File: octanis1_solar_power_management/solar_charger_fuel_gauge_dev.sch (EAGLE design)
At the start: 92 parts, among them IC401 TUSB2046BIRHBIRHB, Q2 32.768kHz, Q4 CSTCR4M00G15L99, Q401 CSTCR6M00G15L99, U1 BQ24210, U2 BQ27510_DRZ_12, U402 TPS62237DRY, U404 TPD2E001DRLR, U6 MSP430F5529IPNR

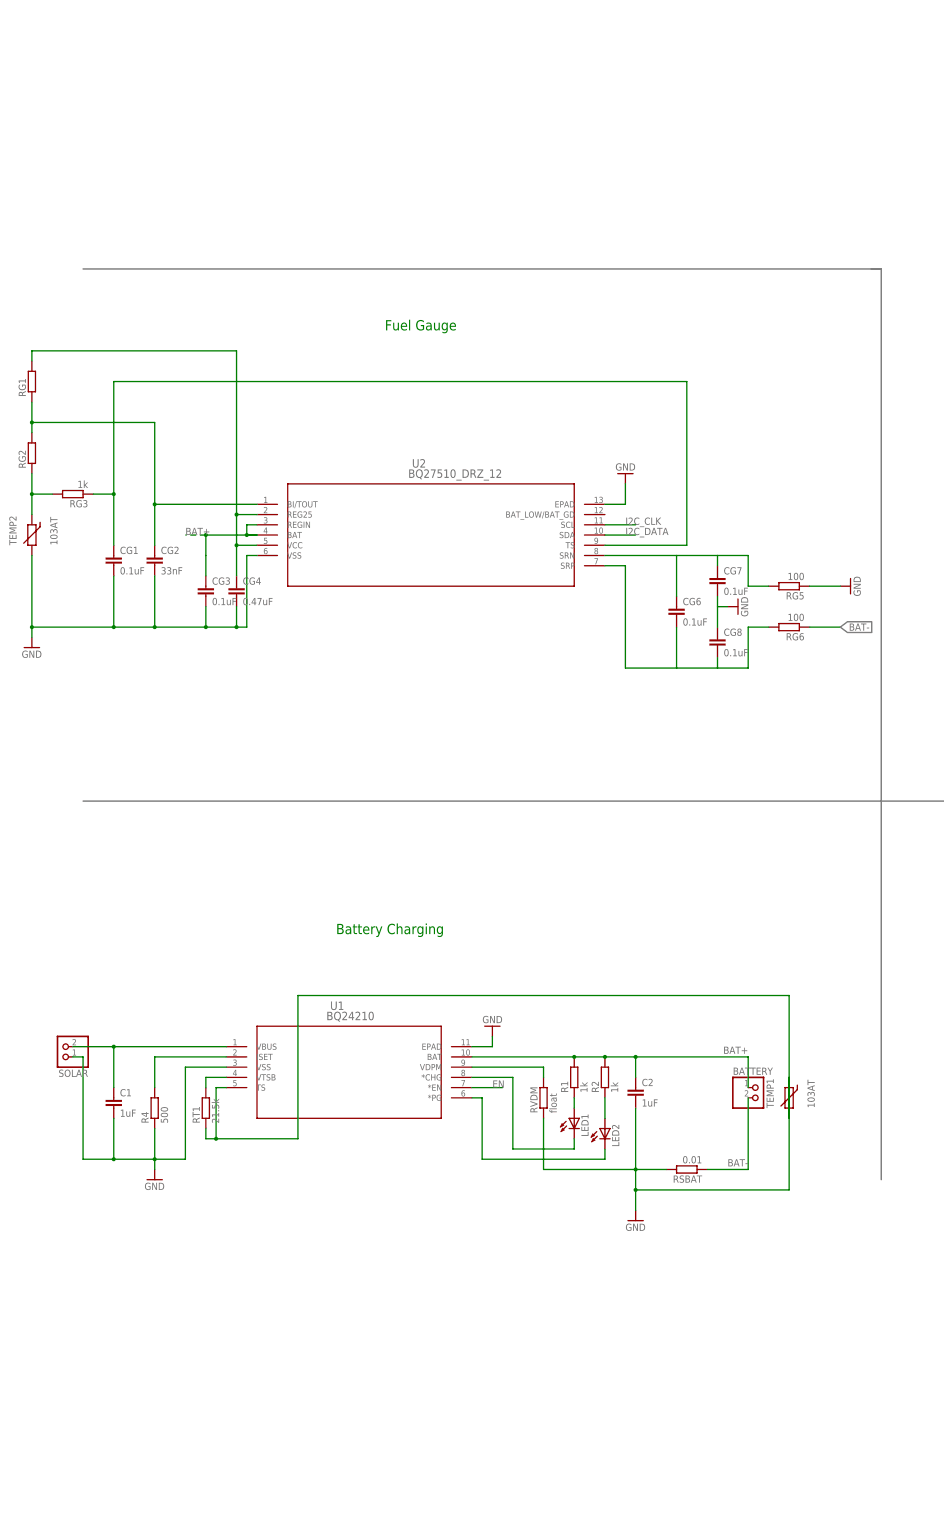
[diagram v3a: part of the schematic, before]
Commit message: changed PCB-size and Added 5V-booster circuit
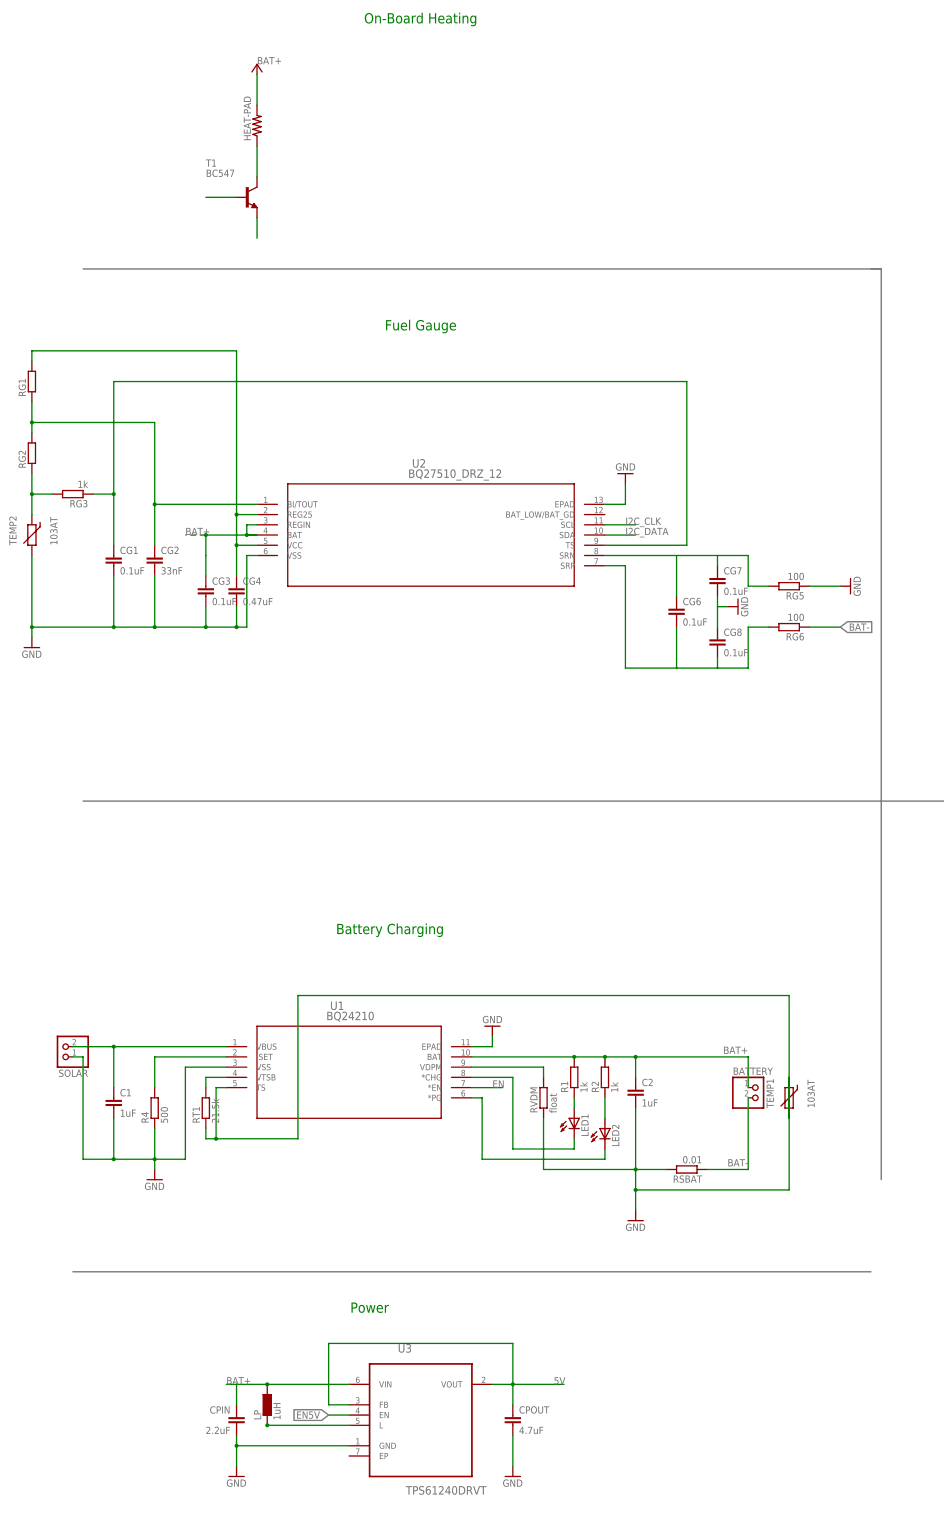
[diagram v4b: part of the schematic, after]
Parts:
- added CPIN: 2.2uF, rcl:C-EUC0805
- added CPOUT: 4.7uF, rcl:C-EUC0805
- added HEAT-PAD: (no value), resistor:R-US_0613/5V
- added LP: 1uH, eagle-ltspice:LL2012C
- added T1: BC547, transistor:BC547
- added U3: TPS61240DRVT, TPS61240DRVT:TPS61240DRVT
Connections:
- new net 5V: CPOUT.1, U3.FB, U3.VOUT
- new net EN5V: U3.EN
- new net N$37: HEAT-PAD.1, T1.C
- new net N$39: T1.E
- new net N$40: T1.B
- new net N$41: LP.2, U3.L
- net +3V3: now also HEAT-PAD.2
- net BAT+: now also CPIN.1, LP.1, U3.VIN
- net GND: now also CPIN.2, CPOUT.2, U3.GND
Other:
- note added: "On-Board Heating"
- note added: "Power"
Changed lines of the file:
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@@
 <part name="CG6" library="rcl" deviceset="C-EU" device="C1206" value="0.1uF"/>
 <part name="GND21" library="supply1" deviceset="GND" device=""/>
+<part name="HEAT-PAD" library="resistor" deviceset="R-US_" device="0613/5V"/>
+<part name="T1" library="transistor" deviceset="BC547" device=""/>
+<part name="BAT+" library="supply1" deviceset="+3V3" device="" value="BAT+"/>
+<part name="U3" library="TPS61240DRVT" deviceset="TPS61240DRVT" device=""/>
+<part name="LP" library="eagle-ltspice" deviceset="L" device="L2012C" value="1uH"/>
+<part name="CPIN" library="rcl" deviceset="C-EU" device="C0805" value="2.2uF"/>
+<part name="CPOUT" library="rcl" deviceset="C-EU" device="C0805" value="4.7uF"/>
+<part name="GND23" library="supply1" deviceset="GND" device=""/>
+<part name="GND24" library="supply1" deviceset="GND" device=""/>
 </parts>
 <sheets>
@@
 <wire x1="481.33" y1="194.31" x2="438.15" y2="194.31" width="0.1524" layer="97" style="shortdash"/>
 <text x="454.66" y="218.44" size="1.778" layer="97">I2C Pull-up Resistor</text>
+<text x="73.66" y="337.82" size="2.54" layer="91" font="fixed" align="bottom-center">On-Board Heating</text>
+<text x="60.96" y="17.78" size="2.54" layer="91" font="fixed" align="bottom-center">Power</text>
+<wire x1="-12.7" y1="27.94" x2="185.42" y2="27.94" width="0.1524" layer="96"/>
 </plain>
 <instances>
@@
 <instance part="CG6" gate="G$1" x="137.16" y="193.04"/>
 <instance part="GND21" gate="1" x="152.4" y="193.04" rot="R90"/>
+<instance part="HEAT-PAD" gate="G$1" x="33.02" y="312.42" rot="R90"/>
+<instance part="T1" gate="G$1" x="30.48" y="294.64"/>
+<instance part="BAT+" gate="G$1" x="33.02" y="327.66" smashed="yes">
+<attribute name="VALUE" x="33.02" y="327.66" size="1.778" layer="96"/>
+</instance>
+<instance part="U3" gate="A" x="73.66" y="-5.08"/>
+<instance part="LP" gate="G$1" x="35.56" y="-5.08"/>
+<instance part="CPIN" gate="G$1" x="27.94" y="-7.62" rot="MR0"/>
+<instance part="CPOUT" gate="G$1" x="96.52" y="-7.62"/>
+<instance part="GND23" gate="1" x="96.52" y="-22.86"/>
+<instance part="GND24" gate="1" x="27.94" y="-22.86"/>
 </instances>
 <busses>
 </busses>
 <nets>
-<net name="GND" class="0">
+<net name="GND" class="4">
 <segment>
 <pinref part="C2" gate="G$1" pin="2"/>
@@
 <wire x1="149.86" y1="193.04" x2="147.32" y2="193.04" width="0.1524" layer="91"/>
 </segment>
+<segment>
+<pinref part="CPOUT" gate="G$1" pin="2"/>
+<wire x1="96.52" y1="-12.7" x2="96.52" y2="-20.32" width="0.1524" layer="91"/>
+<pinref part="GND23" gate="1" pin="GND"/>
+</segment>
+<segment>
+<pinref part="CPIN" gate="G$1" pin="2"/>
+<wire x1="27.94" y1="-12.7" x2="27.94" y2="-15.24" width="0.1524" layer="91"/>
+<pinref part="U3" gate="A" pin="GND"/>
+<wire x1="55.88" y1="-15.24" x2="27.94" y2="-15.24" width="0.1524" layer="91"/>
+<wire x1="27.94" y1="-15.24" x2="27.94" y2="-20.32" width="0.1524" layer="91"/>
+<pinref part="GND24" gate="1" pin="GND"/>
+<junction x="27.94" y="-15.24"/>
+</segment>
 </net>
 <net name="BAT+" class="3">
@@
 <junction x="30.48" y="210.82"/>
 </segment>
+<segment>
+<pinref part="U3" gate="A" pin="VIN"/>
+<wire x1="55.88" y1="0" x2="35.56" y2="0" width="0.1524" layer="91"/>
+<label x="25.4" y="0" size="1.778" layer="95"/>
+<pinref part="LP" gate="G$1" pin="1"/>
+<wire x1="35.56" y1="0" x2="27.94" y2="0" width="0.1524" layer="91"/>
+<junction x="35.56" y="0"/>
+<pinref part="CPIN" gate="G$1" pin="1"/>
+<wire x1="27.94" y1="0" x2="25.4" y2="0" width="0.1524" layer="91"/>
+<wire x1="27.94" y1="-5.08" x2="27.94" y2="0" width="0.1524" layer="91"/>
+</segment>
 </net>
 <net name="N$2" class="0">
@@
 </segment>
 </net>
-<net name="SOLAR" class="0">
+<net name="SOLAR" class="4">
 <segment>
 <pinref part="C1" gate="G$1" pin="2"/>
@@
 <wire x1="459.74" y1="213.36" x2="459.74" y2="210.82" width="0.1524" layer="91"/>
 <junction x="444.5" y="213.36"/>
+</segment>
+<segment>
+<pinref part="HEAT-PAD" gate="G$1" pin="2"/>
+<wire x1="33.02" y1="317.5" x2="33.02" y2="325.12" width="0.1524" layer="91"/>
+<pinref part="BAT+" gate="G$1" pin="+3V3"/>
 </segment>
 </net>
@@
 </segment>
 </net>
-<net name="BAT-" class="0">
+<net name="BAT-" class="4">
 <segment>
 <pinref part="BATTERY" gate="G$1" pin="2"/>
@@
 </segment>
 </net>
+<net name="N$37" class="0">
+<segment>
+<pinref part="HEAT-PAD" gate="G$1" pin="1"/>
+<pinref part="T1" gate="G$1" pin="C"/>
+<wire x1="33.02" y1="307.34" x2="33.02" y2="299.72" width="0.1524" layer="91"/>
+</segment>
+</net>
+<net name="N$39" class="0">
+<segment>
+<pinref part="T1" gate="G$1" pin="E"/>
+<wire x1="33.02" y1="289.56" x2="33.02" y2="284.48" width="0.1524" layer="91"/>
+</segment>
+</net>
+<net name="N$40" class="0">
+<segment>
+<pinref part="T1" gate="G$1" pin="B"/>
+<wire x1="27.94" y1="294.64" x2="20.32" y2="294.64" width="0.1524" layer="91"/>
+</segment>
+</net>
+<net name="N$41" class="0">
+<segment>
+<pinref part="LP" gate="G$1" pin="2"/>
+<pinref part="U3" gate="A" pin="L"/>
+<wire x1="55.88" y1="-10.16" x2="35.56" y2="-10.16" width="0.1524" layer="91"/>
+<junction x="35.56" y="-10.16"/>
+</segment>
+</net>
+<net name="5V" class="3">
+<segment>
+<pinref part="U3" gate="A" pin="VOUT"/>
+<wire x1="91.44" y1="0" x2="96.52" y2="0" width="0.1524" layer="91"/>
+<pinref part="CPOUT" gate="G$1" pin="1"/>
+<wire x1="96.52" y1="0" x2="109.22" y2="0" width="0.1524" layer="91"/>
+<wire x1="96.52" y1="0" x2="96.52" y2="-5.08" width="0.1524" layer="91"/>
+<label x="106.68" y="0" size="1.778" layer="95"/>
+<pinref part="U3" gate="A" pin="FB"/>
+<wire x1="55.88" y1="-5.08" x2="50.8" y2="-5.08" width="0.1524" layer="91"/>
+<wire x1="50.8" y1="-5.08" x2="50.8" y2="10.16" width="0.1524" layer="91"/>
+<wire x1="50.8" y1="10.16" x2="96.52" y2="10.16" width="0.1524" layer="91"/>
+<wire x1="96.52" y1="10.16" x2="96.52" y2="0" width="0.1524" layer="91"/>
+<junction x="96.52" y="0"/>
+</segment>
+</net>
+<net name="EN5V" class="0">
+<segment>
+<pinref part="U3" gate="A" pin="EN"/>
+<wire x1="55.88" y1="-7.62" x2="50.8" y2="-7.62" width="0.1524" layer="91"/>
+<label x="50.8" y="-7.62" size="1.778" layer="95" rot="R180" xref="yes"/>
+</segment>
+</net>

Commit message: added heating circuit
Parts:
- added C3, C5, C6: 22uF, adafruit:C-USC0603K
- added C4: 10nF, adafruit:C-USC0603K
- added JP1, JP2: M021X02_NO_SILK, SparkFun-Connectors:M021X02_NO_SILK
- added L1: 1uH, Coilcraft:XFL4020
- added LED3: (no value), adafruit:LEDCHIPLED_0603
- added R3: 402k, adafruit:R-US_R0603
- added R5: 100k, adafruit:R-US_R0603
- added R6: 1k, adafruit:R-US_R0603
- added R7: 1M, adafruit:R-US_R0603
- added R8: 499k, adafruit:R-US_R0603
- added R9: 0, adafruit:R-US_R0603
- added T2: BC547, transistor:BC547
- added U$1: TPS61230, texas:TPS61230
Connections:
- removed net +3V3: C14.1, C19.2, C30.+, HEAT-PAD.2, R27.2, R28.2, RPUC.2, RPUD.2, S5.P, U6.18, U6.50
- removed net N$13: C1.1, SOLAR.2, U1.VBUS
- removed net N$39: T1.E
- removed net N$40: T1.B
- removed net SOLAR: C1.2, R4.1, SOLAR.1, U1.VSS
- new net IND: L1.2, U$1.SW
- new net N$42: C4.1, U$1.SS
- new net N$43: R3.1, R5.2, U$1.FB
- new net N$44: LED3.C, R6.2
- new net N$45: U$1.EN
- new net N$46: R8.1, R9.2, U$1.HYS
- new net N$47: R7.1, R8.2
- new net SOLAR+: C1.1, C14.1, C19.2, C30.+, R27.2, R28.2, RPUC.2, RPUD.2, S5.P, SOLAR.2, T1.C, U1.VBUS, U6.18, U6.50
- new net VIN: C3.1, L1.1, R7.2, U$1.VIN
- new net VOUT: C5.1, C6.1, JP1.1, JP2.1, LED3.A, R3.2, U$1.VOUT
- net BAT+: now also T2.C
- net GND: now also C1.2, C3.2, C4.2, C5.2, C6.2, HEAT-PAD.1, JP1.2, JP2.2, R4.1, R5.1, R6.1, R9.1, SOLAR.1, U$1.GND, U1.VSS
- net N$37: now also HEAT-PAD.2, T1.E, T2.E; no longer HEAT-PAD.1, T1.C
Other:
- moved on the sheet: HEAT-PAD, T1

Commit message: added heating circuit. added correct step up converter. rearranged components to top layer. drew bigger power traces.
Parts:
- removed CPIN: 2.2uF, rcl:C-EUC0805
- removed CPOUT: 4.7uF, rcl:C-EUC0805
- removed HEAT-PAD: (no value), resistor:R-US_0613/5V
- removed JP1, JP2: M021X02_NO_SILK, SparkFun-Connectors:M021X02_NO_SILK
- removed LP: 1uH, eagle-ltspice:LL2012C
- removed R7: 1M, adafruit:R-US_R0603
- removed R8: 499k, adafruit:R-US_R0603
- removed R9: 0, adafruit:R-US_R0603
- removed U3: TPS61240DRVT, TPS61240DRVT:TPS61240DRVT
- added HEATPAD: 22-23-2021, con-molex:22-23-2021
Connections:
- removed net N$41: LP.2, U3.L
- removed net N$45: U$1.EN
- removed net N$46: R8.1, R9.2, U$1.HYS
- removed net N$47: R7.1, R8.2
- removed net VIN: C3.1, L1.1, R7.2, U$1.VIN
- removed net VOUT: C5.1, C6.1, JP1.1, JP2.1, LED3.A, R3.2, U$1.VOUT
- new net EN_BAT_HEAT: T2.B
- new net EN_SOLAR_HEAT: T1.B
- net 5V: now also C5.1, C6.1, LED3.A, R3.2, U$1.VOUT; no longer CPOUT.1, U3.FB, U3.VOUT
- net BAT+: now also C3.1, L1.1, U$1.VIN; no longer CPIN.1, LP.1, U3.VIN
- net EN5V: now also U$1.EN; no longer U3.EN
- net GND: now also HEATPAD-2.S; no longer CPIN.2, CPOUT.2, HEAT-PAD.1, JP1.2, JP2.2, R9.1, U3.GND
- net N$37: now also HEATPAD-1.S; no longer HEAT-PAD.2
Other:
- note removed: "Power"
- moved on the sheet: C3, TEMP1

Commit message: added H-bridge library
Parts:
- added U3, U4, U5, U7: DRV8836DSSR, DRV8834:DRV8836DSSR
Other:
- moved on the sheet: C3, C4, C5, C6, L1, LED3, R3, R5, R6, U$1

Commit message: arranged power components and h-bridges
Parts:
- added C7, C8: 1uF, rcl:C-EUC0603
- added IC1: REG1117, burr-brown:REG1117
- added SV1, SV2, SV3, SV4: (no value), con-lstb:MA04-1
- C3, C4, C5, C6: device adafruit:C-USC0603K -> rcl:C-EUC0603
- CG1, CG2, CG3, CG4, CG6, CG7, CG8: device rcl:C-EUC1206 -> rcl:C-EUC0603
- R1, R2, RG1, RG2, RG3, RG5, RG6: device resistor:R-EU_R1206 -> rcl:R-EU_R0603
- R3, R5, R6: device adafruit:R-US_R0603 -> rcl:R-EU_R0603
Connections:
- removed net 5V: C5.1, C6.1, LED3.A, R3.2, U$1.VOUT
- new net +3V3: C14.1, C19.2, C30.+, C8.1, IC1.VOUT, R27.2, R28.2, RPUC.2, RPUD.2, S5.P, U6.18, U6.50
- new net M12MODE: U3.MODE
- new net M12SLEEP: U3.NSLEEP
- new net M1IN1: U3.AIN1_/_APHASE
- new net M1IN2: U3.AIN2_/_AENBL
- new net M2IN1: U3.BIN1_/_BPHASE
- new net M2IN2: U3.BIN2_/_BENBL
- new net M34MODE: U4.MODE
- new net M34SLEEP: U4.NSLEEP
- new net M3IN1: U4.AIN1_/_APHASE
- new net M3IN2: U4.AIN2_/_AENBL
- new net M4IN1: U4.BIN1_/_BPHASE
- new net M4IN2: U4.BIN2_/_BENBL
- new net M56MODE: U5.MODE
- new net M56SLEEP: U5.NSLEEP
- new net M5IN1: U5.AIN1_/_APHASE
- new net M5IN2: U5.AIN2_/_AENBL
- new net M6IN1: U5.BIN1_/_BPHASE
- new net M6IN2: U5.BIN2_/_BENBL
- new net M78MODE: U7.MODE
- new net M78SLEEP: U7.NSLEEP
- new net M7IN1: U7.AIN1_/_APHASE
- new net M7IN2: U7.AIN2_/_AENBL
- new net M8IN1: U7.BIN1_/_BPHASE
- new net M8IN2: U7.BIN2_/_BENBL
- new net N$13: SV2.1, U4.AOUT1
- new net N$39: SV2.2, U4.AOUT2
- new net N$40: SV2.3, U4.BOUT1
- new net N$41: SV2.4, U4.BOUT2
- new net N$45: SV3.1, U5.AOUT1
- new net N$46: SV3.2, U5.AOUT2
- new net N$47: SV3.3, U5.BOUT1
- new net N$48: SV3.4, U5.BOUT2
- new net N$49: SV1.1, U3.AOUT1
- new net N$50: SV1.2, U3.AOUT2
- new net N$51: SV1.3, U3.BOUT1
- new net N$52: SV1.4, U3.BOUT2
- new net N$53: SV4.1, U7.AOUT1
- new net N$54: SV4.2, U7.AOUT2
- new net N$55: SV4.3, U7.BOUT1
- new net N$56: SV4.4, U7.BOUT2
- net +5V: now also C5.1, C6.1, LED3.A, R3.2, U$1.VOUT, U3.VCC, U4.VCC, U5.VCC, U7.VCC
- net BAT+: now also C7.1, IC1.VIN
- net GND: now also C7.2, C8.2, IC1.GND, U3.EPAD, U3.GND, U4.EPAD, U4.GND, U5.EPAD, U5.GND, U7.EPAD, U7.GND
- net SOLAR+: no longer C14.1, C19.2, C30.+, R27.2, R28.2, RPUC.2, RPUD.2, S5.P, U6.18, U6.50
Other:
- moved on the sheet: U3, U4, U5, U7
